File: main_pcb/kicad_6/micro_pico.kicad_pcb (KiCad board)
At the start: 4 copper layers, 134.6 x 113 mm, 320 parts, among them J101 PJ301M-12, J102 PJ301M-12, J103 PJ301M-12, J104 PJ301M-12, J105 PJ301M-12, J106 PJ301M-12, J107 PJ-011A, J1201 aux_PWM_in, J1301 aux_VCF_FM_in, J201 aux_FM_in, J301 aux_FM_in, J501 aux_AM_in, J701 white_noise, P101 VCF_plug_in_port, Q1001 MMBT3904, Q701 2N3904, Q801 MMBT3904, Q901 MMBT3904, SW101 SW_SPDT_CO, SW201 SR1712F-0204, SW301 SR1712F-0204, SW701 SW_SPDT_CO, SW801 SW_SPDT_CO, U1 SSI2130, U10 LF398_SOIC14, U11 CD4053, U12 TL072, U13 LM555xM, U14 CD4052B, U1401 LT3467A, U1402 L78L05_SOT89, U1403 LM4040C-2.5, U1404 LM4040C-2.5, U15 TL072, U16 LM555xM, U17 CD4052B, U2 SSI2130, U3 TL072, U4 TL072, U5 TL072, U6 TL072, U7 TL072, U9 SSI2162

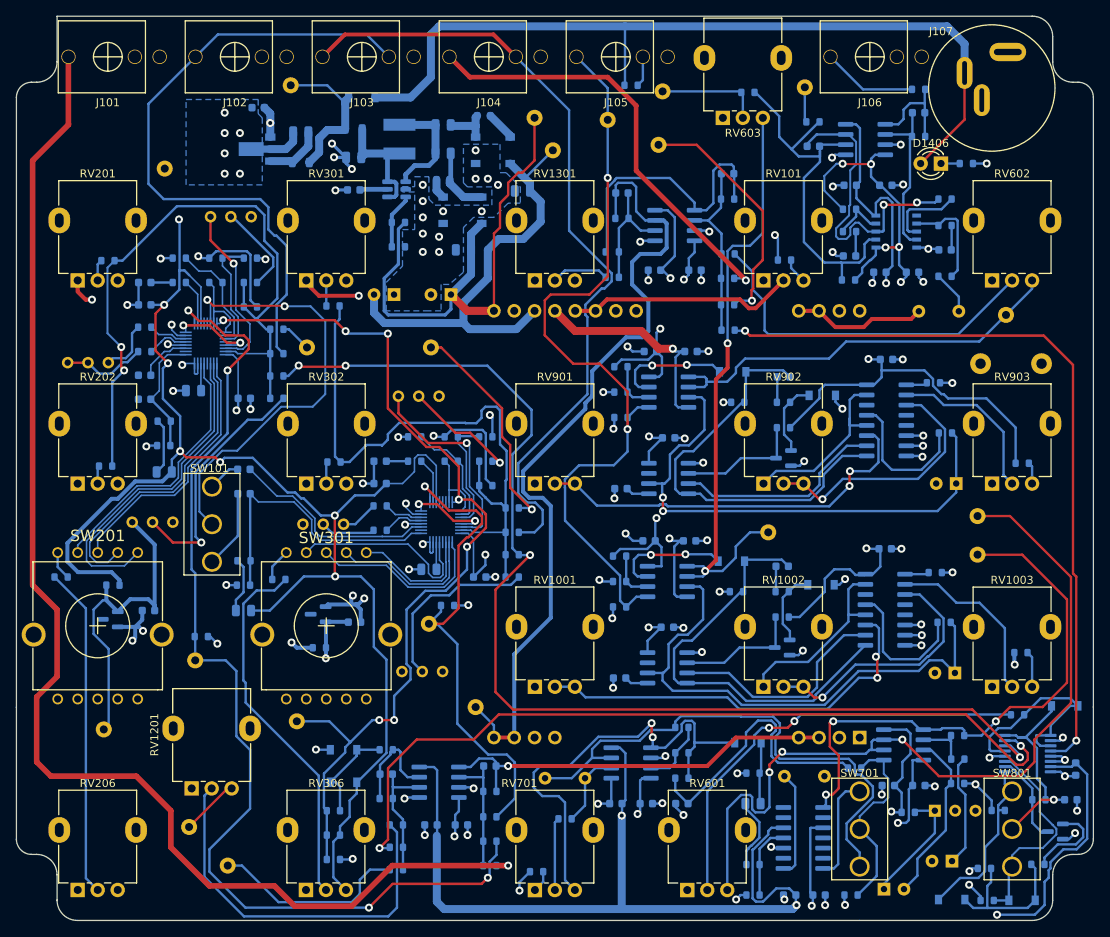
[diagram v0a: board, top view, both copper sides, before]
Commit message: Update rev 0.1, fix VCA tails, add local 2v5 regs, change some pot footprints
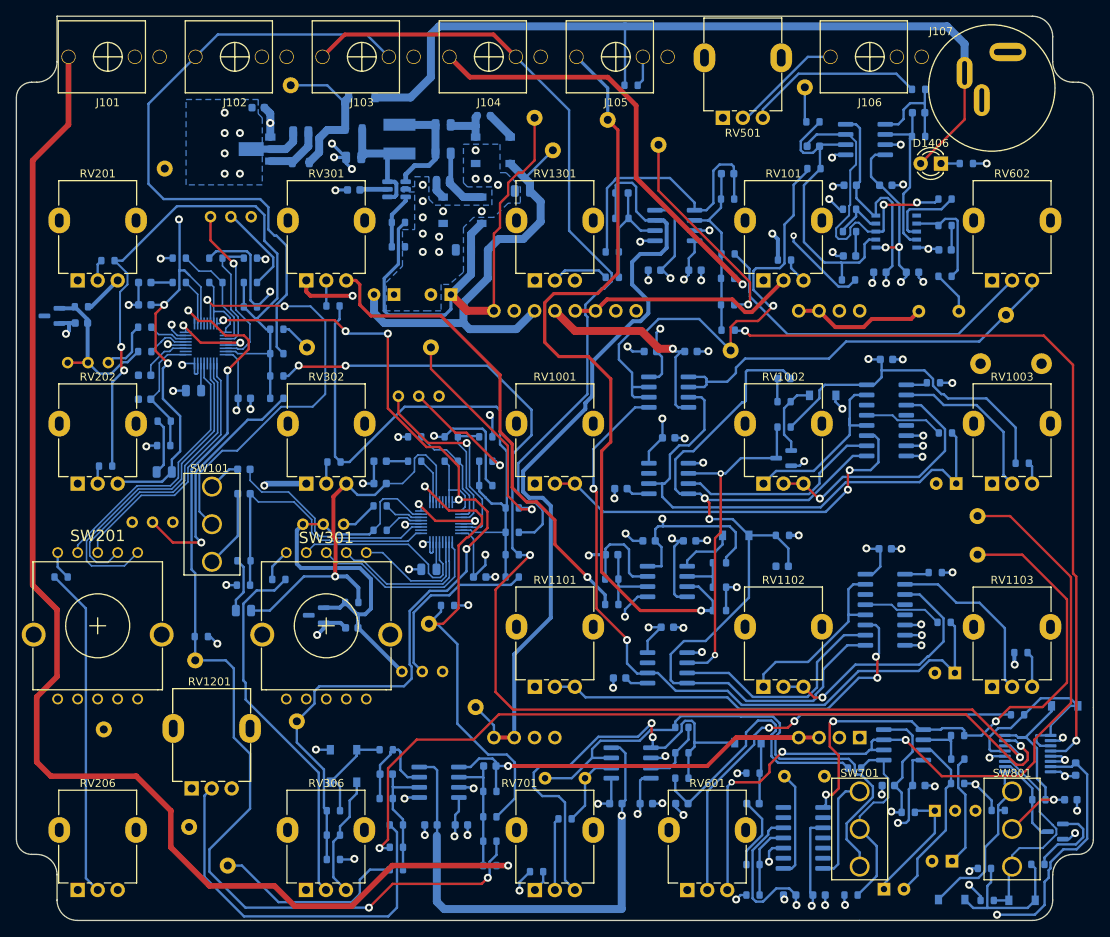
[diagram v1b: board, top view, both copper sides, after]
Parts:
- removed C1412: 100n, Capacitor_SMD:C_0603_1608Metric
- removed D1001, D1002: 1N4148W, Diode_SMD:D_SOD-123
- removed Q1001: MMBT3904, Package_TO_SOT_SMD:SOT-23
- removed R1001: 12k, Resistor_SMD:R_0603_1608Metric
- removed R1002: 100k, Resistor_SMD:R_0603_1608Metric
- removed the R1003 at (149.1, 98.0)
- removed the R1004 at (163.7, 102.4)
- removed the R1005 at (169.4, 102.4)
- removed R1006: 10k, Resistor_SMD:R_0603_1608Metric
- removed RV603: 100k, custom_footprints:Alpha_RD901F
- removed TP109: VCA_AM_CV, TestPoint:TestPoint_Keystone_5000-5004_Miniature
- removed U1403, U1404: LM4040C-2.5, Package_TO_SOT_SMD:SOT-23
- removed kibuzzard-62EE6B91: G***, kibuzzard-62EE6B91
- added C208: 100n, Capacitor_SMD:C_0603_1608Metric, B.Cu at (81.8, 68.8)
- added C308: 100n, Capacitor_SMD:C_0603_1608Metric, B.Cu at (115.6, 106.9)
- added R220: 1k, Resistor_SMD:R_0603_1608Metric, B.Cu at (81.8, 66.8)
- added R320: 1k, Resistor_SMD:R_0603_1608Metric, B.Cu at (115.6, 103.8)
- added RV501: 5k, custom_footprints:Bourns_PTV09, F.Cu at (162.0, 43.2)
- added U201: LM4040C-2.5, Package_TO_SOT_SMD:SOT-23, B.Cu at (78.1, 67.9)
- added U301: LM4040C-2.5, Package_TO_SOT_SMD:SOT-23, B.Cu at (111.1, 105.4)
- C703: value 2n2 -> 1n; footprint Capacitor_SMD:C_0805_2012Metric -> Capacitor_SMD:C_0603_1608Metric
- D1406: value LED -> XLMDK65D
- R101: value 1k -> 10k
- R1203: value 100k -> 220k
- R1304: value 68k -> 56k
- R1307: value 120k -> 220k
- R1405: value 390 -> 100k
- R1406: value 6k8 -> 100k
- R203, R303: value 33k -> 39k
- R204, R304: value 100k -> 200k
- R205, R305, R702: value 1M -> 2M2
- R504: value 270k -> 100k
- R505: value 33k -> 27k
- R508: value 33k -> 12k
- R509: value 1k -> 270
- R710: value 5k6 -> 12k
- R711: value 1k8 -> 4k7
- R901: value 12k -> 100k
- R902: value 100k -> 12k
- RV101: value 100k -> 10k
- RV1201: value 100k -> 5k; footprint custom_footprints:Alpha_RD901F -> custom_footprints:Bourns_PTV09
- moved R1405 62.4 mm to (148.1, 104.0), turned to 0 degrees
- moved C1411 58.3 mm to (148.1, 97.8)
- moved R1406 37.5 mm to (148.1, 100.8)
- moved R901 30.0 mm to (161.5, 104.8)
- moved R903 27.4 mm to (161.5, 98.8), turned to 0 degrees
- moved R902 24.5 mm to (161.5, 101.9)
- moved kibuzzard-62EE6A9F 23.2 mm to (168.8, 72.3)
- moved TP601 23.2 mm to (162.9, 72.3)
- moved D901 20.5 mm to (163.6, 95.4)
- moved R904 17.6 mm to (169.4, 95.4), turned to 0 degrees
- moved kibuzzard-62EC6A5B 16.8 mm to (115.6, 77.2)
- moved R502 12.6 mm to (173.4, 49.5)
- moved kibuzzard-62EC6A3A 10.6 mm to (116.0, 112.4)
- moved kibuzzard-62EE65B4 0.46 mm to (168.7, 32.4)
- moved C901 0.22 mm to (169.6, 75.8)
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- renumbered C902 to C1002, C903 to C1003, C1003 to C1004, C1004 to C1005, C904 to C1006, C905 to C1007, C1001 to C1101, C1002 to C1102, C1005 to C1103, C1103 to C1104, C1104 to C1105, C1006 to C1106, C1007 to C1107, R907 to R1003, R909 to R1004, R908 to R1005, R1007 to R1103, R1009 to R1104, R1008 to R1105, RV901 to RV1001, RV902 to RV1002, RV903 to RV1003, RV1001 to RV1101, RV1002 to RV1102, RV1003 to RV1103
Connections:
- C1101 pad 1: Net-(C1001-Pad1) -> /CV_generators/VCA_env/GATE
- C1103 pad 1: Net-(C1005-Pad1) -> Net-(C1103-Pad1)
- C1411 pad 1: +2V5_REF -> Net-(C1411-Pad1)
- C1411 pad 2: GND -> -5V_REF
- C901 pad 1: Net-(C901-Pad1) -> /CV_generators/VCA_env/GATE
- D901 pad 1: Net-(C901-Pad1) -> /CV_generators/VCA_env/GATE
- Q901 pad 3: Net-(Q901-Pad3) -> /CV_generators/VCA_env/~{TRIG}
- R101 pad 1: +2V5_REF -> +5V
- R1105 pad 2: Net-(C1005-Pad1) -> Net-(C1103-Pad1)
- R1405 pad 2: +2V5_REF -> Net-(C1411-Pad1)
- R1406 pad 1: -2V5_REF -> Net-(C1411-Pad1)
- R1406 pad 2: -12V -> -5V_REF
- R203 pad 2: +2V5_REF -> /VCO_A/LOCAL_2V5_REF
- R213 pad 2: +2V5_REF -> /VCO_A/LOCAL_2V5_REF
- R217 pad 2: +2V5_REF -> /VCO_A/LOCAL_2V5_REF
- R303 pad 2: +2V5_REF -> /VCO_B/LOCAL_2V5_REF
- R313 pad 2: +2V5_REF -> /VCO_B/LOCAL_2V5_REF
- R317 pad 2: +2V5_REF -> /VCO_B/LOCAL_2V5_REF
- R504 pad 2: -12V -> -5V_REF
- R509 pad 1: /VCA/SIGNAL_OUT -> Net-(C505-Pad1)
- R509 pad 2: Net-(C505-Pad1) -> Net-(R509-Pad2)
- R510 pad 2: -12V -> -5V_REF
- R901 pad 1: GND -> /CV_generators/GATE_IN
- R901 pad 2: Net-(R901-Pad2) -> GND
- R902 pad 1: /CV_generators/GATE_IN -> GND
- R902 pad 2: GND -> Net-(R902-Pad2)
- R903 pad 1: Net-(R901-Pad2) -> Net-(R902-Pad2)
- R904 pad 1: Net-(C901-Pad1) -> /CV_generators/VCA_env/GATE
- R906 pad 2: Net-(Q901-Pad3) -> /CV_generators/VCA_env/~{TRIG}
- RV1201 pad 3: -2V5_REF -> -5V_REF
- RV1301 pad 3: -2V5_REF -> -5V_REF
- RV201 pad 1: -2V5_REF -> -5V_REF
- RV201 pad 3: +2V5_REF -> +5V
- RV202 pad 1: -2V5_REF -> -5V_REF
- RV202 pad 3: +2V5_REF -> +5V
- RV203 pad 3: +2V5_REF -> /VCO_A/LOCAL_2V5_REF
- RV204 pad 2: +2V5_REF -> /VCO_A/LOCAL_2V5_REF
- RV204 pad 3: +2V5_REF -> /VCO_A/LOCAL_2V5_REF
- RV301 pad 1: -2V5_REF -> -5V_REF
- RV301 pad 3: +2V5_REF -> +5V
- RV302 pad 1: -2V5_REF -> -5V_REF
- RV302 pad 3: +2V5_REF -> +5V
- RV303 pad 3: +2V5_REF -> /VCO_B/LOCAL_2V5_REF
- RV304 pad 2: +2V5_REF -> /VCO_B/LOCAL_2V5_REF
- RV304 pad 3: +2V5_REF -> /VCO_B/LOCAL_2V5_REF
- TP601 pad 1: /CV_generators/VCA_env/OUT -> /CV_generators/VCA_CV
- U1 pad 23: +2V5_REF -> /VCO_A/LOCAL_2V5_REF
- U12 pad 5: /CV_generators/GATE_IN -> Net-(C1103-Pad1)
- U12 pad 6: Net-(R901-Pad2) -> /CV_generators/VCA_CV
- U12 pad 7: Net-(D901-Pad2) -> /CV_generators/VCA_CV
- U13 pad 2: Net-(Q901-Pad3) -> /CV_generators/VCA_env/~{TRIG}
- U13 pad 4: Net-(C901-Pad1) -> /CV_generators/VCA_env/GATE
- U14 pad 9: Net-(C901-Pad1) -> /CV_generators/VCA_env/GATE
- U15 pad 1: /CV_generators/VCA_env/OUT -> Net-(D901-Pad2)
- U15 pad 2: /CV_generators/VCA_env/OUT -> Net-(R902-Pad2)
- U15 pad 3: Net-(C1005-Pad1) -> /CV_generators/GATE_IN
- U15 pad 5: /CV_generators/GATE_IN -> GND
- U15 pad 6: Net-(R1001-Pad2) -> Net-(C1411-Pad1)
- U15 pad 7: Net-(D1001-Pad2) -> -5V_REF
- U16 pad 2: Net-(Q1001-Pad3) -> /CV_generators/VCA_env/~{TRIG}
- U16 pad 4: Net-(C1001-Pad1) -> /CV_generators/VCA_env/GATE
- U16 pad 6: Net-(C1005-Pad1) -> Net-(C1103-Pad1)
- U17 pad 9: Net-(C1001-Pad1) -> /CV_generators/VCA_env/GATE
- U2 pad 23: +2V5_REF -> /VCO_B/LOCAL_2V5_REF
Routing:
- net +2V5_REF: track 328.9 -> 0.00 mm, vias 5 -> 0
- net -5V_REF: track 0.00 -> 290.5 mm, vias 0 -> 5
- net -2V5_REF: track 204.2 -> 0.00 mm, vias 3 -> 0
- net +5V: track 371.9 -> 538.1 mm, vias 9 -> 8
- net /CV_generators/VCA_env/GATE: track 0.00 -> 121.9 mm, vias 0 -> 2
- net Net-(C1103-Pad1): track 0.00 -> 90.3 mm, vias 0 -> 2
- net /VCO_B/LOCAL_2V5_REF: track 0.00 -> 89.7 mm, vias 0 -> 1
- net /VCO_A/LOCAL_2V5_REF: track 0.00 -> 87.9 mm, vias 0 -> 2
- net /CV_generators/VCA_env/OUT: track 77.1 -> 0.00 mm, vias 2 -> 0
- net Net-(C1005-Pad1): track 65.6 -> 0.00 mm
- net Net-(C1001-Pad1): track 53.3 -> 0.00 mm
- net Net-(C901-Pad1): track 52.7 -> 0.00 mm
- net /CV_generators/VCA_CV: track 13.2 -> 60.6 mm, vias 0 -> 1
- net /CV_generators/VCA_env/~{TRIG}: track 0.00 -> 42.5 mm, vias 0 -> 2
- net -12V: track 537.3 -> 506.6 mm, vias 16 -> 13
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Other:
- board text added: "rev 0.1 2022-08-28"
- board text removed: "rev 0.1 2022-08-18"

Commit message: Change 555 timer type, fixes odd ADSR behavior
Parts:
- U13, U16: value LM555xM -> TLC555
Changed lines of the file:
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@@
       (effects (font (size 1 1) (thickness 0.15)) (justify mirror))
     )
-    (fp_text value "LM555xM" (at 0 -3.4) (layer "B.Fab")
+    (fp_text value "TLC555" (at 0 -3.4) (layer "B.Fab")
       (effects (font (size 1 1) (thickness 0.15)) (justify mirror))
     )
@@
     (property "Sheetfile" "power_supply.kicad_sch")
     (property "Sheetname" "power_supply")
-    (attr smd exclude_from_pos_files exclude_from_bom)
+    (attr smd exclude_from_pos_files)
     (fp_text reference "R1403" (at 0 -1.4478) (layer "B.SilkS")
       (effects (font (size 1 1) (thickness 0.15)) (justify mirror))
@@
     (property "Sheetfile" "power_supply.kicad_sch")
     (property "Sheetname" "power_supply")
-    (attr smd exclude_from_pos_files exclude_from_bom)
+    (attr smd exclude_from_pos_files)
     (fp_text reference "R1404" (at 0 1.27) (layer "B.SilkS")
       (effects (font (size 1 1) (thickness 0.15)) (justify mirror))
@@
       (effects (font (size 1 1) (thickness 0.15)) (justify mirror))
     )
-    (fp_text value "LM555xM" (at 0 -3.4) (layer "B.Fab")
+    (fp_text value "TLC555" (at 0 -3.4) (layer "B.Fab")
       (effects (font (size 1 1) (thickness 0.15)) (justify mirror))
     )

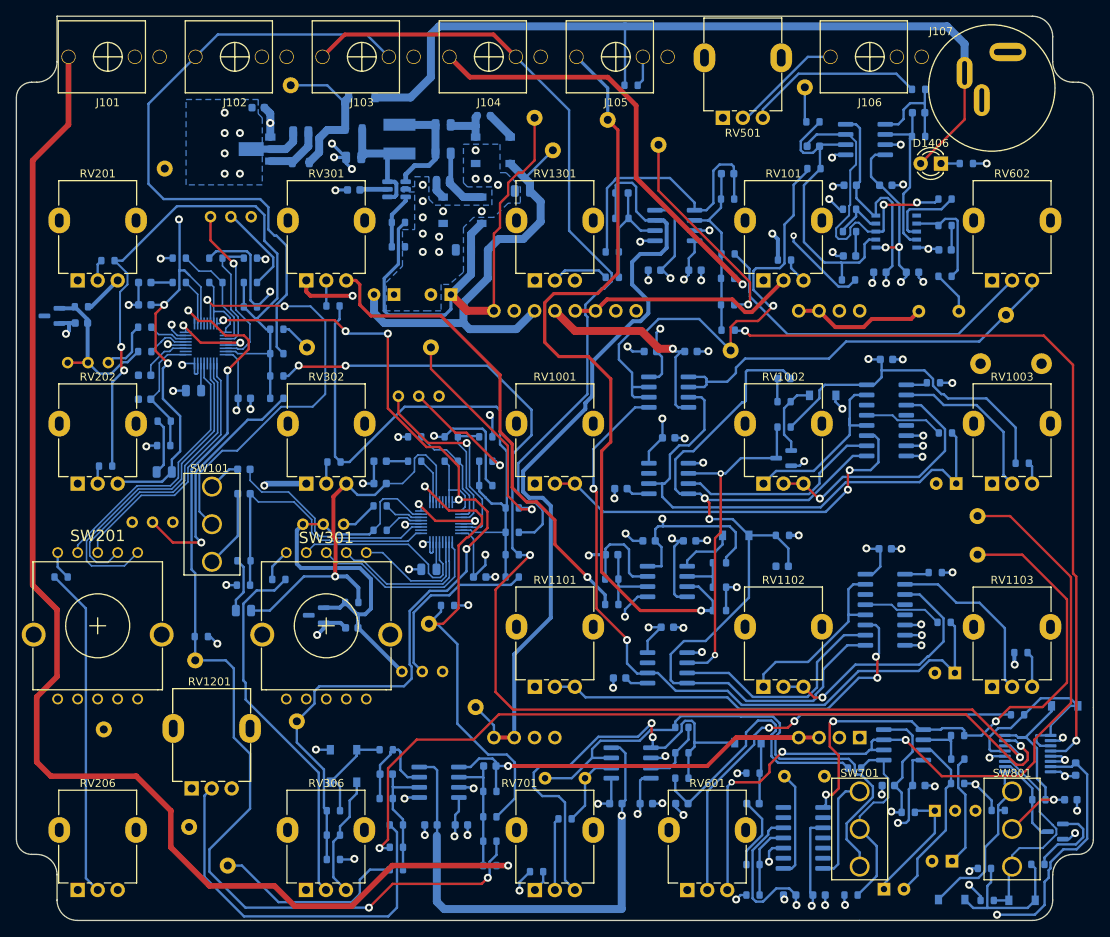
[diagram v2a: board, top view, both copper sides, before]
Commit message: Add mod-wheel VCA, fix occasional VCO freq locking
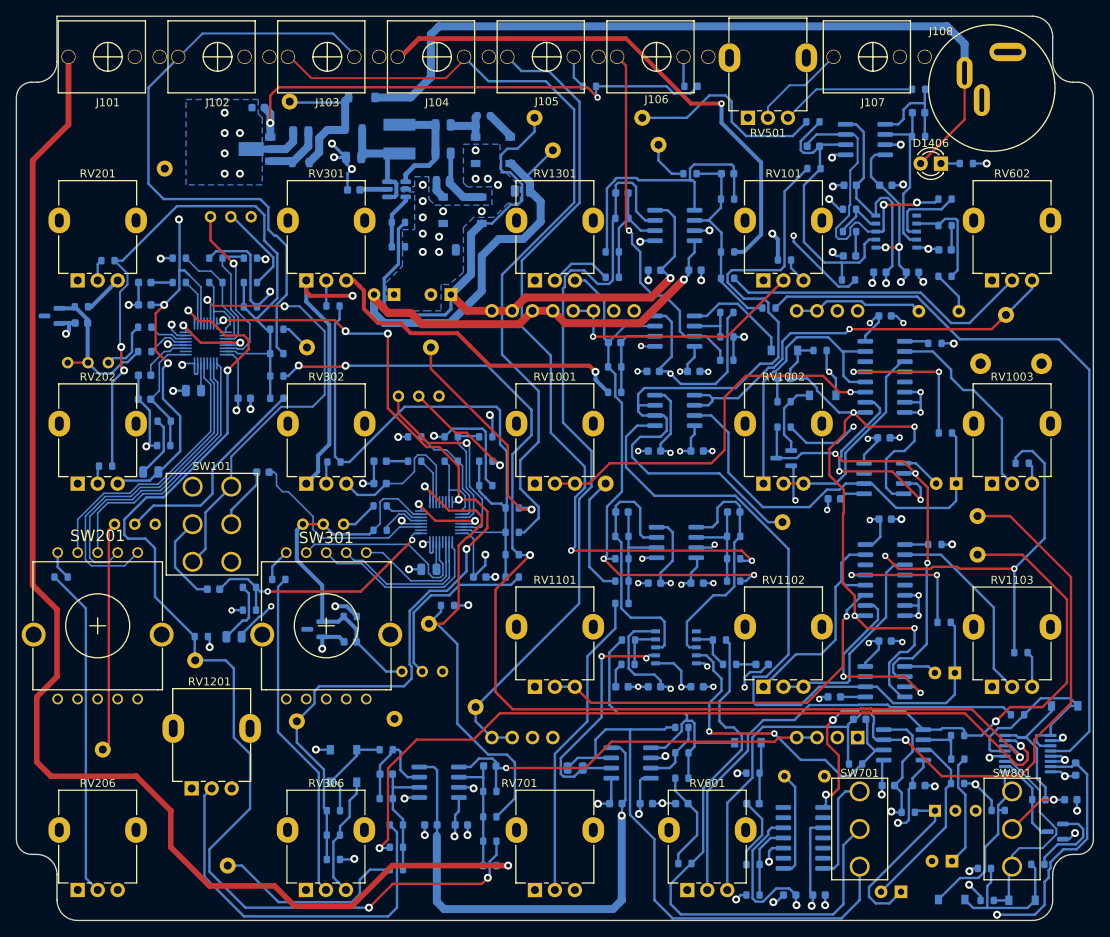
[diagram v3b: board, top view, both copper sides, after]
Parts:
- removed C1101: 100p, Capacitor_SMD:C_0603_1608Metric
- removed the R714 at (178.0, 140.3)
- removed TP101: GATE_IN, TestPoint:TestPoint_Keystone_5000-5004_Miniature
- removed TP1405: +2V5, TestPoint:TestPoint_Keystone_5000-5004_Miniature
- removed TP1406: -2V5, TestPoint:TestPoint_Keystone_5000-5004_Miniature
- removed kibuzzard-62EE6B71: G***, kibuzzard-62EE6B71
- removed kibuzzard-62EE6FC7: G***, kibuzzard-62EE6FC7
- removed kibuzzard-62EE6FFA: G***, kibuzzard-62EE6FFA
- added C701: 1n, Capacitor_SMD:C_0603_1608Metric, B.Cu at (149.4, 114.3)
- added C703: 1n, Capacitor_SMD:C_0603_1608Metric, B.Cu at (149.4, 92.5)
- added C707: 1n, Capacitor_SMD:C_0603_1608Metric, B.Cu at (166.9, 111.5)
- added C708: 100p, Capacitor_SMD:C_0603_1608Metric, B.Cu at (179.1, 118.4)
- added C709: 1n, Capacitor_SMD:C_0603_1608Metric, B.Cu at (163.3, 92.5)
- added C718: 100n, Capacitor_SMD:C_0603_1608Metric, B.Cu at (153.4, 101.3)
- added C719: 100n, Capacitor_SMD:C_0603_1608Metric, B.Cu at (158.8, 101.3)
- added C720: 100n, Capacitor_SMD:C_0603_1608Metric, B.Cu at (153.4, 114.3)
- added C721: 100n, Capacitor_SMD:C_0603_1608Metric, B.Cu at (158.8, 114.3)
- added J105: PJ301M-12, custom_footprints:PJ301M-12, F.Cu at (140.0, 35.6)
- added J702: aux_LFO_FM_in, TestPoint:TestPoint_Keystone_5000-5004_Miniature, B.Cu at (147.3, 88.9)
- added R101: 1k, Resistor_SMD:R_0603_1608Metric, B.Cu at (145.3, 39.2)
- added R702: 22k, Resistor_SMD:R_0603_1608Metric, B.Cu at (150.2, 108.5)
- added R703: 270, Resistor_SMD:R_0603_1608Metric, B.Cu at (150.1, 111.5)
- added R705: 68k, Resistor_SMD:R_0603_1608Metric, B.Cu at (149.4, 98.3)
- added R708: 39k, Resistor_SMD:R_0603_1608Metric, B.Cu at (149.4, 95.5)
- added R715: 100k, Resistor_SMD:R_0603_1608Metric, B.Cu at (161.5, 108.5)
- added R716: 270, Resistor_SMD:R_0603_1608Metric, B.Cu at (162.8, 111.5)
- added R717: 100k, Resistor_SMD:R_0603_1608Metric, B.Cu at (178.6, 124.0)
- added R718: 100k, Resistor_SMD:R_0603_1608Metric, B.Cu at (163.3, 101.1)
- added R719: 100k, Resistor_SMD:R_0603_1608Metric, B.Cu at (163.3, 98.3)
- added R720: 56k, Resistor_SMD:R_0603_1608Metric, B.Cu at (163.3, 95.5)
- added TP201: 2V5, TestPoint:TestPoint_Keystone_5000-5004_Miniature, B.Cu at (84.5, 122.1)
- added TP301: 2V5, TestPoint:TestPoint_Keystone_5000-5004_Miniature, B.Cu at (120.9, 118.3)
- added U18: TL072, Package_SO:SOIC-8_3.9x4.9mm_P1.27mm, B.Cu at (156.2, 96.3)
- added U19: SSI2162, Package_SO:SSOP-10_3.9x4.9mm_P1.00mm, B.Cu at (156.1, 109.4)
- added kibuzzard-633F7F05: G***, kibuzzard-633F7F05, B.Cu at (154.9, 88.9)
- added kibuzzard-634019ED: G***, kibuzzard-634019ED, B.Cu at (89.0, 122.2)
- added kibuzzard-634019F6: G***, kibuzzard-634019F6, B.Cu at (125.6, 118.3)
- C702: renamed from C704; value 220n -> 10n; footprint Capacitor_THT:C_Rect_L7.0mm_W3.5mm_P5.00mm -> Capacitor_SMD:C_0805_2012Metric
- Q701: value 2N3904 -> 2N3904_wide
- R701: renamed from R705; value 270k -> 220k
- R707: value 100 -> 200k
- RV701: value 100k A -> 100k
- SW101: value SW_SPDT_CO -> SW_DP_on_on_on; footprint custom_footprints:SPDT_mini_toggle -> custom_footprints:DPDT_mini_toggle
- moved R707 37.9 mm to (149.4, 101.1)
- moved R901 31.3 mm to (162.5, 73.5)
- moved R902 31.3 mm to (162.5, 70.6)
- moved R903 31.3 mm to (162.5, 67.5)
- moved U15 31.3 mm to (156.0, 69.8)
- moved R706 27.8 mm to (149.4, 103.9)
- moved C1107 27.3 mm to (182.2, 108.6)
- moved U16 27.3 mm to (182.2, 113.7)
- moved C1102 26.9 mm to (175.9, 115.6)
- moved C1007 26.9 mm to (182.1, 83.2)
- moved U13 26.9 mm to (182.1, 88.3)
- moved C1002 26.7 mm to (175.9, 90.8)
- moved C1411 26.5 mm to (148.4, 71.3)
- moved R1405 26.5 mm to (148.5, 77.5)
- moved R1406 26.5 mm to (148.5, 74.3)
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- renumbered C703 to C704, C706 to C705, C705 to C706, C701 to C710, C702 to C711, C707 to C712, C708 to C713, C709 to C714, C710 to C715, C711 to C716, C712 to C717, J105 to J106, J106 to J107, J107 to J108, R101 to R103, R709 to R706, R708 to R709, R712 to R713, R713 to R714, R701 to R721, R702 to R722, R703 to R723, R706 to R724
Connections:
- net /CV_generators/LFO/SAMPLE_AND_HOLD renamed /CV_generators/LFO/S&H
- C202 pad 2: /VCO_A/SOFT_SYNC_IN -> GND
- C203 pad 2: /VCO_A/HARD_SYNC_IN -> GND
- C702 pad 1: Net-(C704-Pad1) (its old number) -> Net-(C702-Pad1)
- J106 pad 2: Net-(J105-Pad2) -> Net-(J106-Pad2)
- R102 pad 1: /RAW_9VDC -> Net-(J106-Pad2)
- R102 pad 2: Net-(J105-Pad2) -> +5V
- R706 pad 2: Net-(C704-Pad1) (its old number) -> Net-(C703-Pad2)
- R707 pad 1: Net-(R707-Pad1) -> Net-(C703-Pad2)
- R707 pad 2: GND -> Net-(J702-Pad1)
- RV701 pad 1: Net-(R707-Pad1) -> GND
- RV701 pad 3: /CV_generators/LFO/RAW_SQUARE -> +5V
- SW101 pad 1: /VCO_B/HARD_SYNC_IN -> /VCO_A_PULSE
- SW101 pad 2: /VCO_A_PULSE -> /VCO_B/HARD_SYNC_IN
- SW101 pad 3: /VCO_B/SOFT_SYNC_IN -> GND
- U6 pad 6: Net-(C704-Pad1) (its old number) -> Net-(C702-Pad1)
- U7 pad 5: /CV_generators/LFO/HI_Z_SQUARE -> GND
- U7 pad 6: /CV_generators/LFO/OUT -> Net-(C708-Pad2)
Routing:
- net /CV_generators/LFO_DEPTH_CV: track 0.00 -> 99.1 mm, vias 0 -> 2
- net +5V: track 538.1 -> 611.3 mm, vias 8 -> 10
- net /CV_generators/GATE_IN: track 100.6 -> 45.6 mm
- net /CV_generators/LFO/HI_Z_SQUARE: track 24.4 -> 72.1 mm
- net Net-(C708-Pad2): track 0.00 -> 43.1 mm, vias 0 -> 2
- net GND: track 187.3 -> 225.1 mm, vias 109 -> 108
- net /CV_generators/VCA_env/GATE: track 121.9 -> 86.9 mm, vias 2 -> 4
- net +12V: track 567.0 -> 601.5 mm, vias 12 -> 16
- net /CV_generators/VCA_CV: track 60.6 -> 93.7 mm, vias 1 -> 0
- net Net-(C703-Pad1): track 0.00 -> 32.6 mm
- net Net-(C702-Pad1): track 0.00 -> 30.7 mm, vias 0 -> 2
- net Net-(C709-Pad1): track 0.00 -> 30.4 mm
- net /VCO_A/LOCAL_2V5_REF: track 87.9 -> 117.9 mm
- net Net-(R706-Pad1): track 9.08 -> 39.0 mm
- net Net-(C706-Pad1): track 34.6 -> 12.8 mm
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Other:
- board text added: "rev 1.0 2022-10-06"
- board text removed: "rev 0.1 2022-08-28"
